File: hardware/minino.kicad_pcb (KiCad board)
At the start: 2 copper layers, 42 x 68 mm, 51 parts, among them J1 OLED, J2 GPS, J3 Battery, P1 USB_C_Plug_USB2.0, Q1 DMG3415U-7, SW1 ON, SW2 RIGHT, SW3 LEFT, SW4 DOWN, SW5 UP, SW6 OK, SW7 RESET, SW8 GPIO, U1 ESP32-S3-WROOM-1U-N16, U2 MCP73831-3-OT, U3 AP2112K-3.3

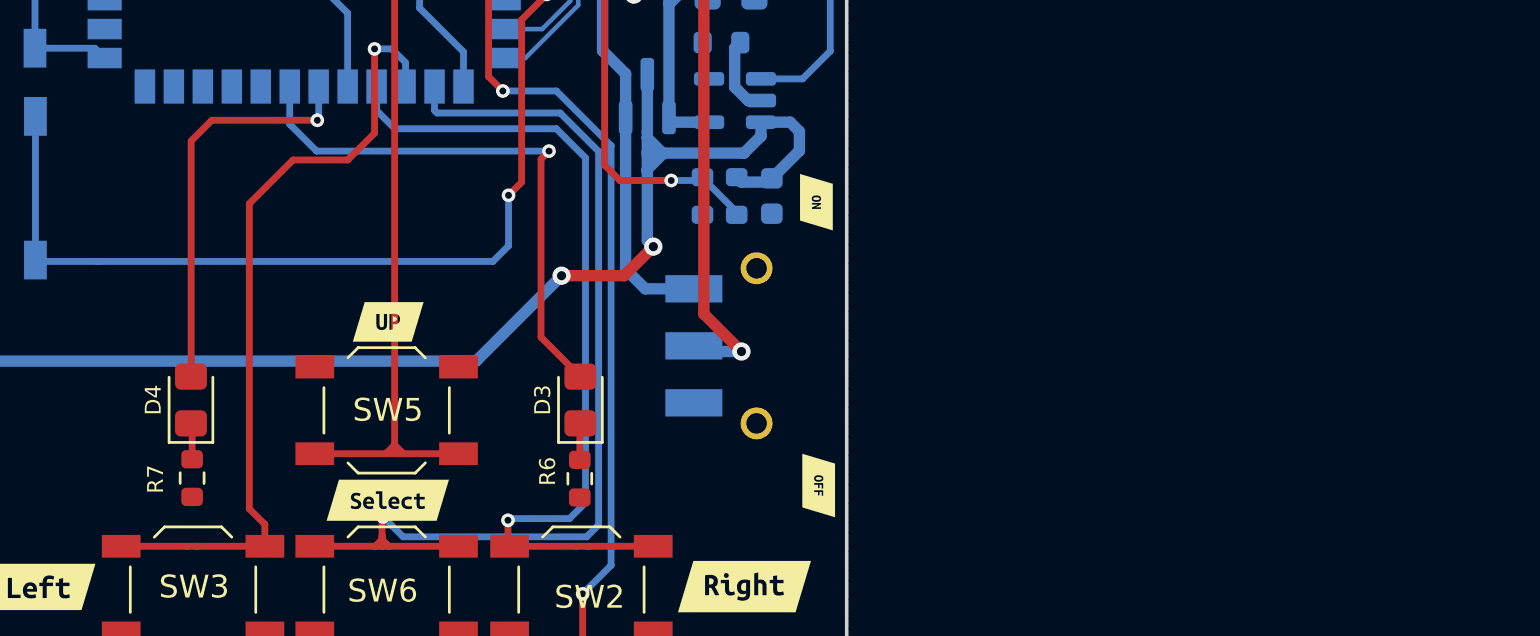
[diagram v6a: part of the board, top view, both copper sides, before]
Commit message: Add_Buzz
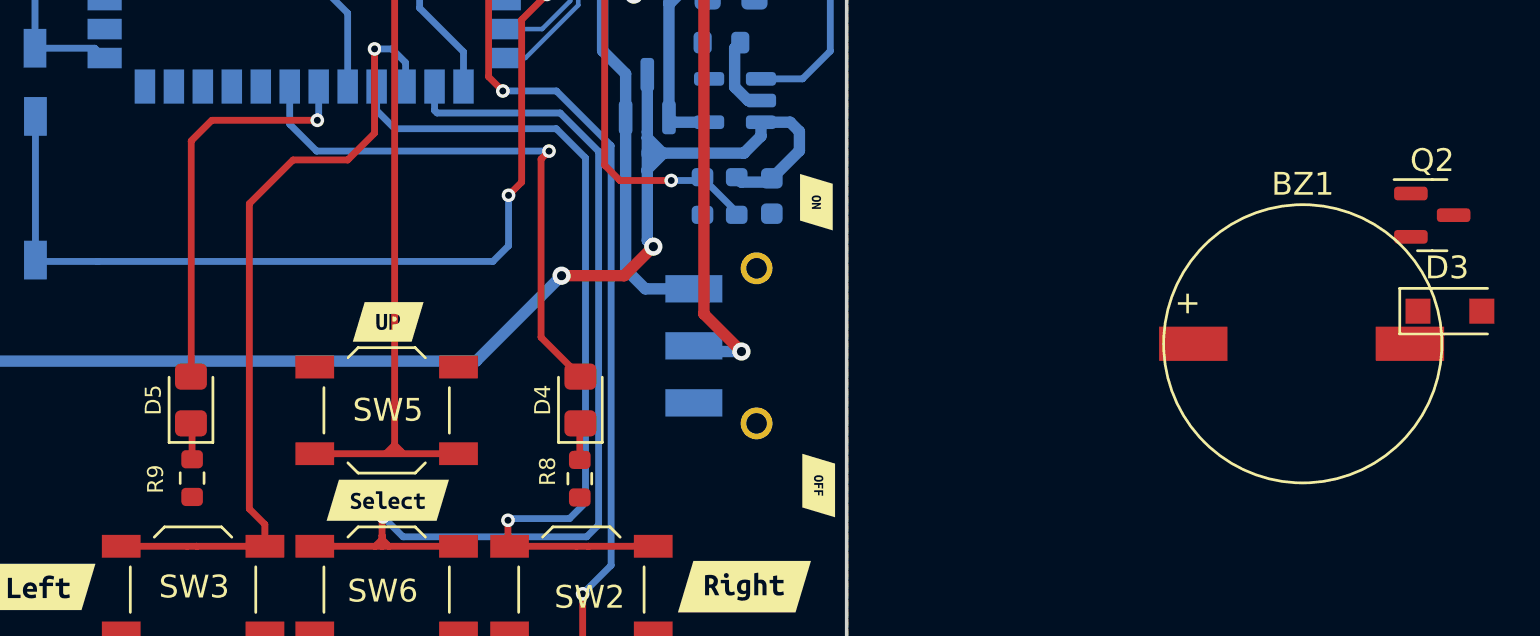
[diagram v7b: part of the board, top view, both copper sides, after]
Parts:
- removed G***: LOGO, Aesthetics:electronic_cats_logo_8x6
- removed REF**: OSHW-Symbol_6.7x6mm_Copper, Symbol:OSHW-Symbol_6.7x6mm_Copper
- added BZ1: Buzzer, Buzzer_Beeper:MagneticBuzzer_ProSignal_ABI-009-RC, F.Cu at (109.2, 82.9)
- added D3: MBR120, Diode_SMD:D_SOD-123F, F.Cu at (119.5, 81.4)
- added Q2: PN2222A, Package_TO_SOT_SMD:SOT-23, F.Cu at (118.7, 77.2)
- renumbered C3 to C2, C4 to C3, C2 to C4, D3 to D4, D4 to D5, R8 to R10, R9 to R11, R10 to R12, R6 to R8, R7 to R9
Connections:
- U1 pad 19: /D1 -> /DIO11
- U1 pad 22: unconnected-(U1-Pad22) -> /Buzz

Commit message: Update_design
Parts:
- added R6: 1.1K, Resistor_SMD:R_0603_1608Metric_Pad0.98x0.95mm_HandSolder, B.Cu at (180.8, 75.5)
- added R7: 10K, Resistor_SMD:R_0603_1608Metric_Pad0.98x0.95mm_HandSolder, B.Cu at (182.2, 75.5)
- added Ref**: Val**, Aesthetics:01.PCB, F.Cu at (257.7, 152.6)
- BZ1: footprint Buzzer_Beeper:MagneticBuzzer_ProSignal_ABI-009-RC -> Footprint:CAPAE1050X250N; moved to B.Cu
- D3, Q2: moved to B.Cu
- moved SW7 149.6 mm to (200.4, 38.6), turned to 180 degrees
- moved J3 124.3 mm to (176.0, 66.7), turned to 90 degrees
- moved kibuzzard-6397B251 120.8 mm to (176.4, 70.2), turned to -90 degrees
- moved SW8 120.4 mm to (172.6, 38.5), turned to 180 degrees
- moved C3 119.8 mm to (201.4, 48.8)
- moved C2 119.8 mm to (199.9, 48.8)
- moved R12 119.8 mm to (200.7, 51.1)
- moved C4 119.8 mm to (198.4, 48.8)
- moved R10 119.5 mm to (199.4, 76.8), turned to 180 degrees
- moved P1 119.3 mm to (201.4, 83.4)
- moved R11 118.7 mm to (197.2, 85.7), turned to 0 degrees
- moved U1 118.7 mm to (187.8, 56.4)
- moved kibuzzard-6397B263 118.0 mm to (173.1, 70.3), turned to -90 degrees
- moved D2 117.6 mm to (203.7, 72.1)
- moved F1 117.3 mm to (203.1, 76.1), turned to 90 degrees
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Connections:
- J2 pad 5: /D1 -> /DIO11
- P1 pad S1: unconnected-(P1-PadS1) -> GND
- U1 pad 20: /LED1 -> /LED2
- U1 pad 21: /LED2 -> /LED1
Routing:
- net /RST: track 58.1 -> 28.9 mm, vias 2 -> 0
- net /D1: track 28.7 -> 0.00 mm, vias 1 -> 0
- net /DIO11: track 0.00 -> 26.9 mm, vias 0 -> 1
- net /BOOT: track 9.53 -> 36.3 mm
- net VBUS: track 29.7 -> 56.1 mm
- net Net-(BZ1-Pad2): track 0.00 -> 25.6 mm
- net +BATT: track 55.5 -> 31.1 mm, vias 2 -> 1
- net +3V3: track 70.3 -> 93.5 mm, vias 1 -> 3
- net Net-(D2-Pad1): track 24.6 -> 43.3 mm, vias 0 -> 4
- net unconnected-(P1-PadS1): track 16.9 -> 0.00 mm
- net /Buzz: track 0.00 -> 14.0 mm
- net /SELECT: track 44.0 -> 36.6 mm
- net /SCL: track 11.0 -> 18.1 mm
- net /D-: track 25.1 -> 31.7 mm, vias 0 -> 2
- net /B_ADC: track 20.4 -> 25.6 mm, vias 2 -> 0
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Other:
- board size 42 x 68 mm -> 45 x 68 mm
